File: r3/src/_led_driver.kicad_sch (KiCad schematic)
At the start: 4 parts, among them J16 FH12A-20S-0.5SH, U17 PCA9685PW

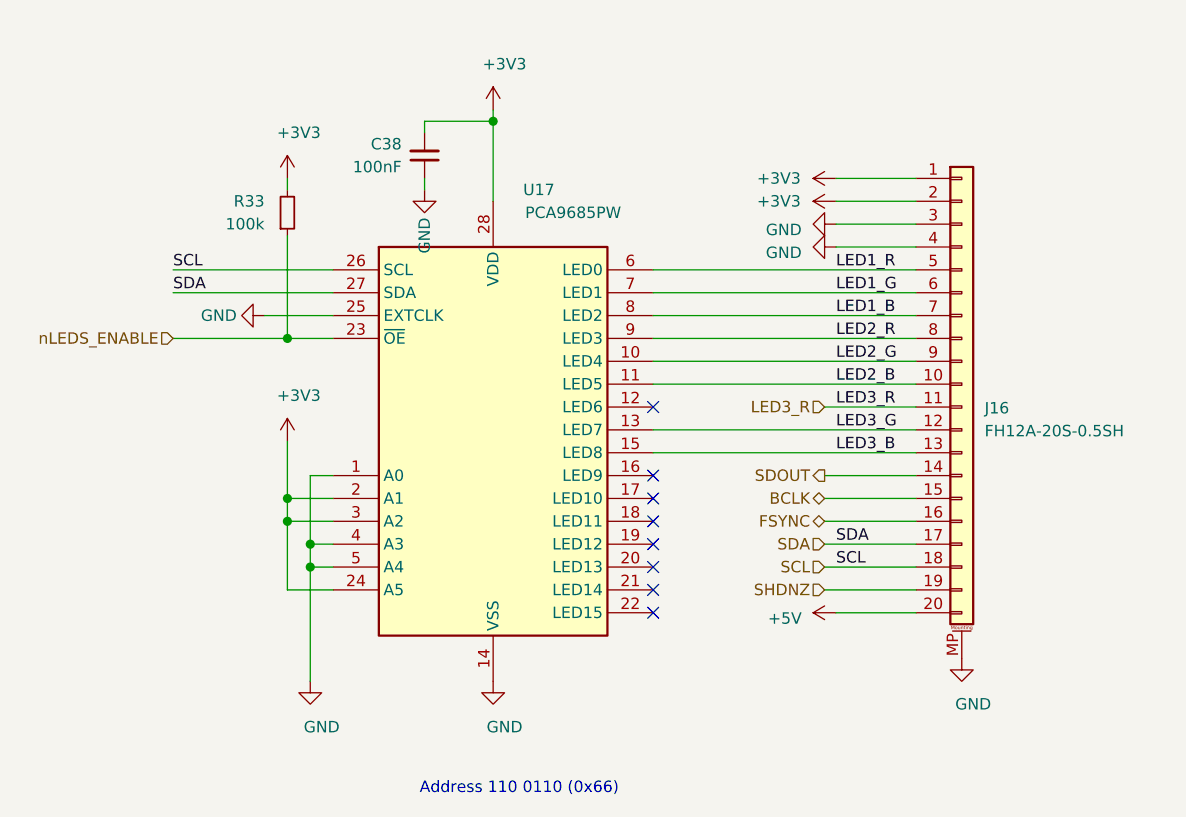
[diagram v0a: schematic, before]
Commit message: Replace LED driver with PCF8574 IO expander. There was some weird interference between the LED PWM signals and the I2S bus, plus the stupid thing initialised with the LED's full white.
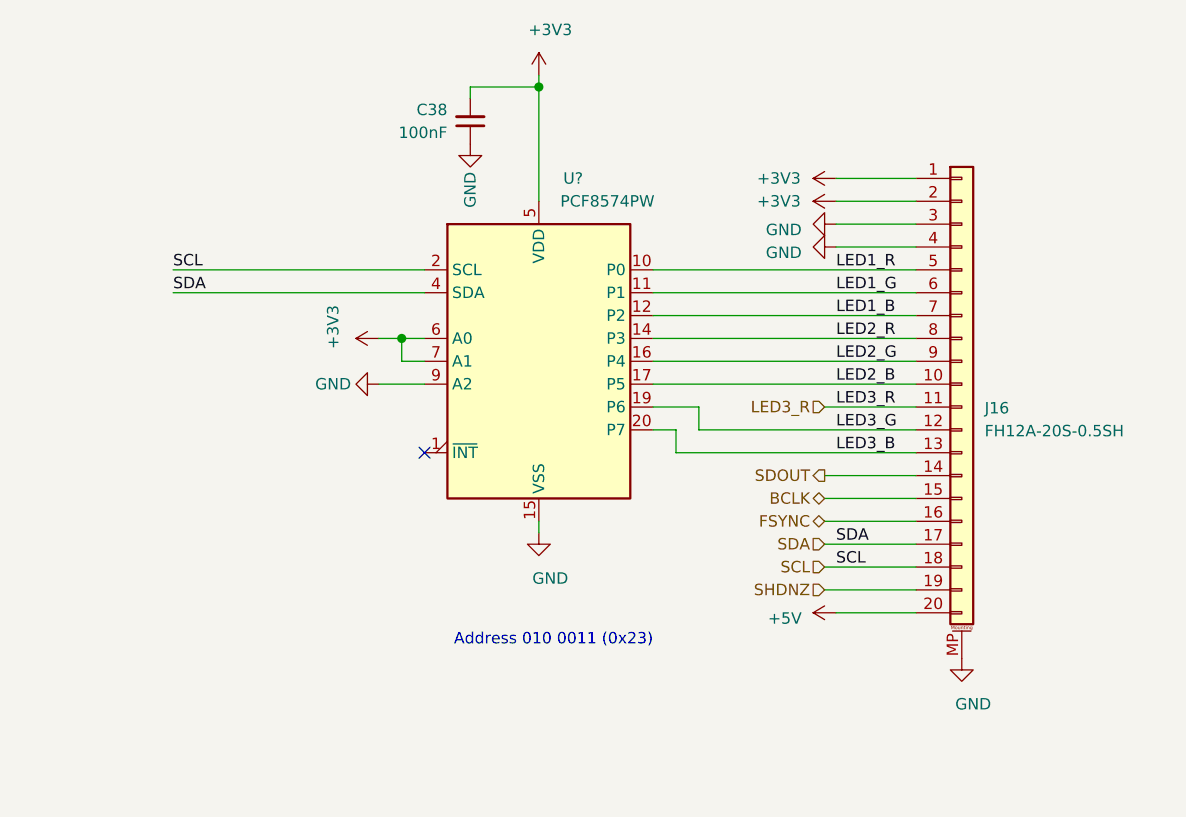
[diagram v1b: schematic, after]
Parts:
- removed R33: 100k, Resistor_SMD:R_0603_1608Metric, symbol Device:R_Small
- removed U17: PCA9685PW, Package_SO:TSSOP-28_4.4x9.7mm_P0.65mm, symbol Driver_LED:PCA9685PW
- added U?: PCF8574PW, Package_SO:SSOP-20_4.4x6.5mm_P0.65mm, symbol Interface_Expansion:PCF8574TS
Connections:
- net +3V3: now also U?.5 (VDD), U?.6 (A0), U?.7 (A1)
- net GND: now also U?.15 (VSS), U?.9 (A2)
- net LED1_B: now also U?.12 (P2)
- net LED1_G: now also U?.11 (P1)
- net LED1_R: now also U?.10 (P0)
- net LED2_B: now also U?.17 (P5)
- net LED2_G: now also U?.16 (P4)
- net LED2_R: now also U?.14 (P3)
- net LED3_B: now also U?.20 (P7)
- net LED3_G: now also U?.19 (P6)
- net SCL: now also U?.2 (SCL)
- net SDA: now also U?.4 (SDA)
- no-connect marks 8 -> 1
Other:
- note added: "Address 010 0011 (0x23)"
- note removed: "Address 110 0110 (0x66)"
- moved on the sheet: C38

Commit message: Annotate PCF8574
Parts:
- gave numbers to parts that had none: 1
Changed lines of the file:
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@@
   (symbol (lib_id "Interface_Expansion:PCF8574TS") (at 142.24 69.85 0) (unit 1)
     (in_bom yes) (on_board yes)
-    (property "Reference" "U?" (id 0) (at 146.05 49.53 0))
+    (property "Reference" "U9" (id 0) (at 146.05 49.53 0))
     (property "Value" "PCF8574PW" (id 1) (at 149.86 52.07 0))
     (property "Footprint" "Package_SO:SSOP-20_4.4x6.5mm_P0.65mm" (id 2) (at 142.24 69.85 0)
